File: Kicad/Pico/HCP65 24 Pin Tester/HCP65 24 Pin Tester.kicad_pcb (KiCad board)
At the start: 2 copper layers, 92 x 81.8 mm, 64 parts, among them IC1 SN74ABT245BDBR, IC2 SN74ABT245BDBR, IC3 SN74ABT245BDBR, J1 6339167-2, J3 Conn_01x12_Socket, J8 Conn_01x12_Socket, J9 Conn_01x12_Socket

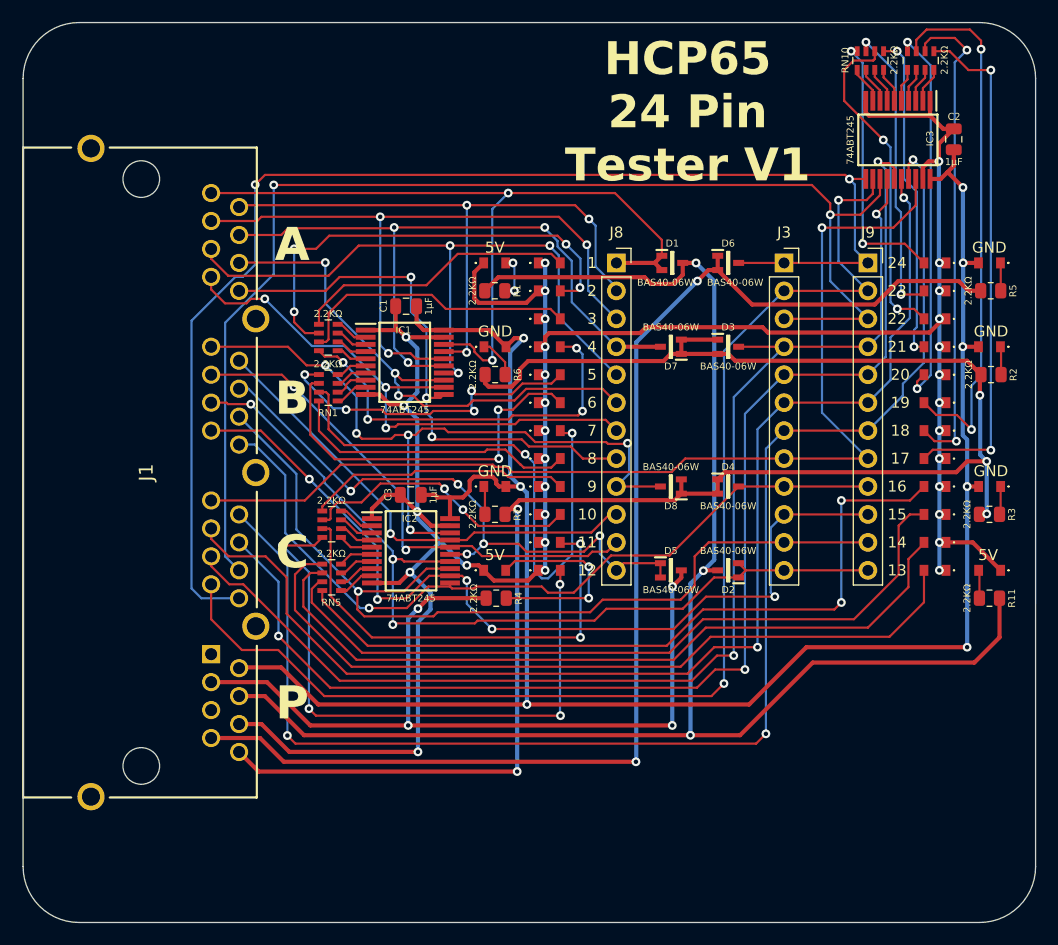
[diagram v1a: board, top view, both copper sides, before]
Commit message: Generated Gerbers for 24pin Tester.
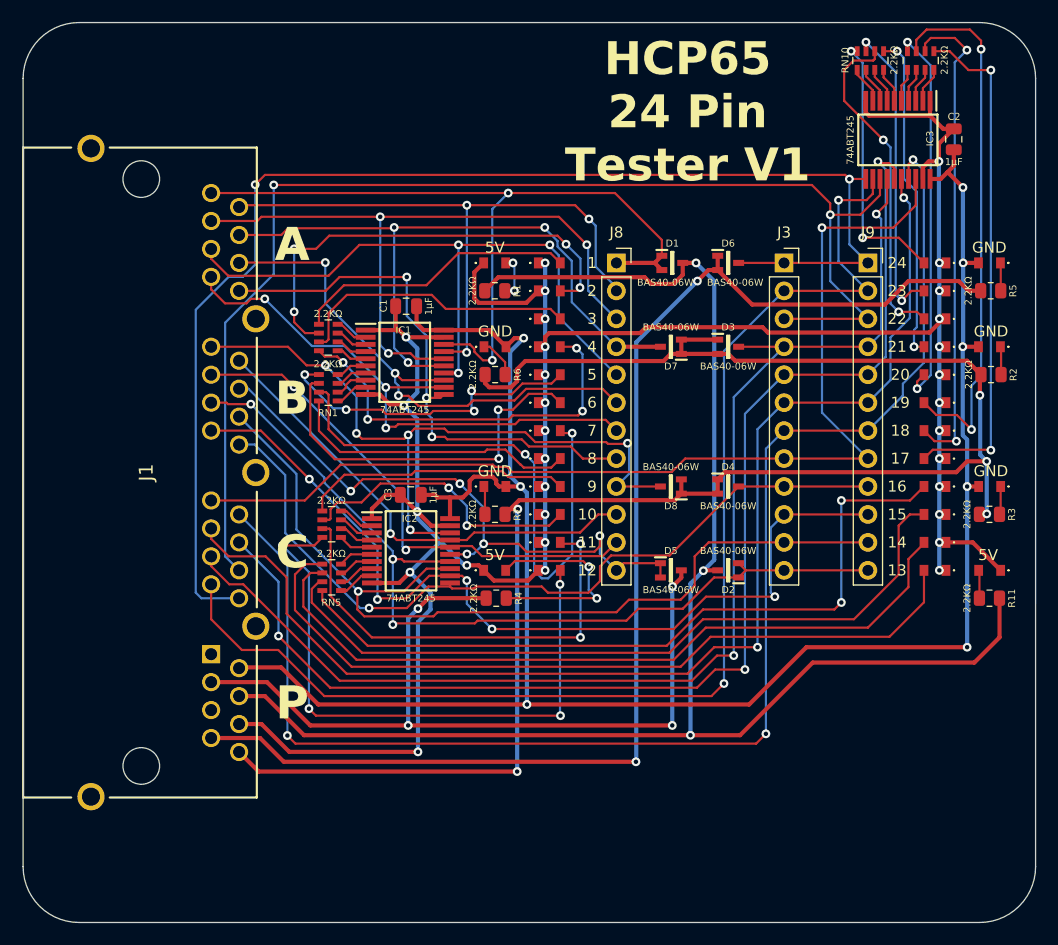
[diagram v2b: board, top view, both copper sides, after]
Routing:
- net Net-(LED5-Pad2): track 18.5 -> 19.5 mm
- net /S9: track 25.7 -> 26.5 mm
- net /IO15: track 71.9 -> 72.7 mm
- net /S22: track 27.3 -> 28.1 mm
- net /IO11: track 55.0 -> 55.7 mm
- net /IO9: track 42.5 -> 43.2 mm
- net /S8: track 24.0 -> 24.5 mm

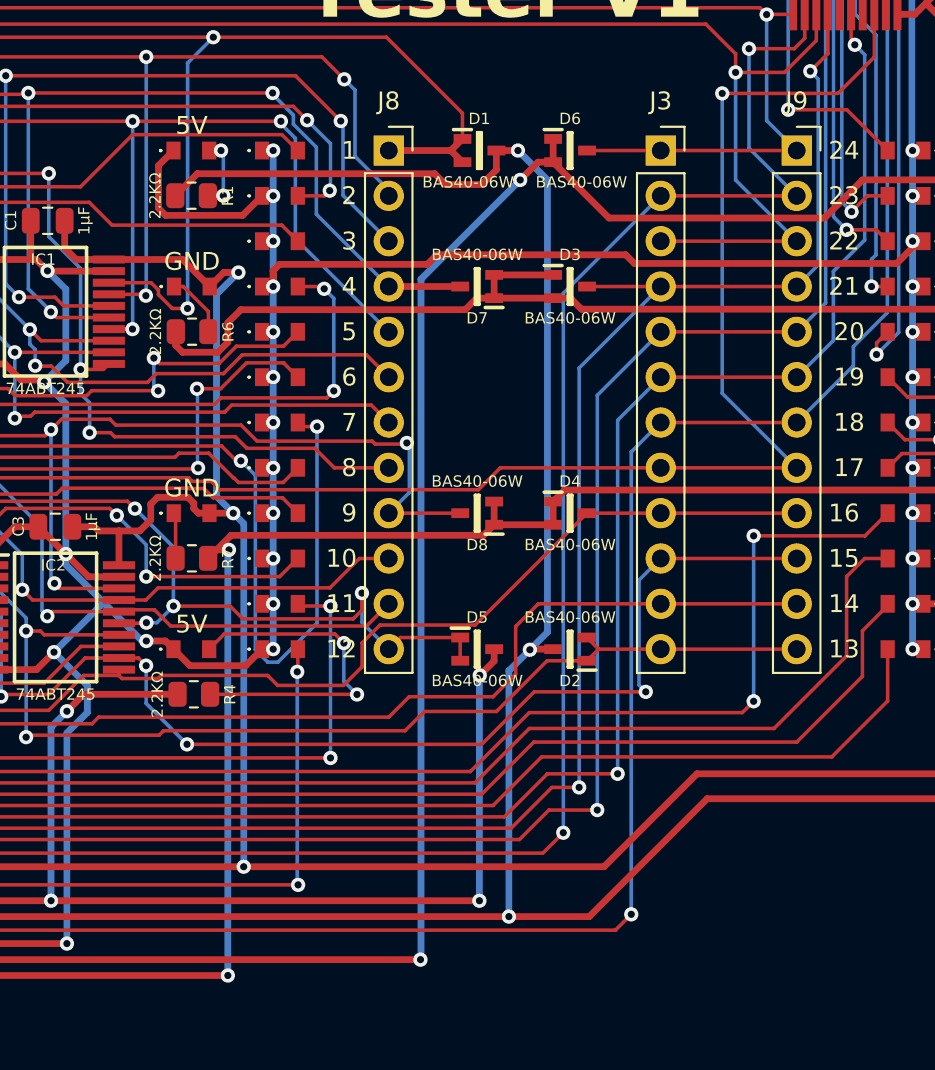
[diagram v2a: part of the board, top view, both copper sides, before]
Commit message: Added board alignment silk screen to 24- 32- and 40 pin tester boards.
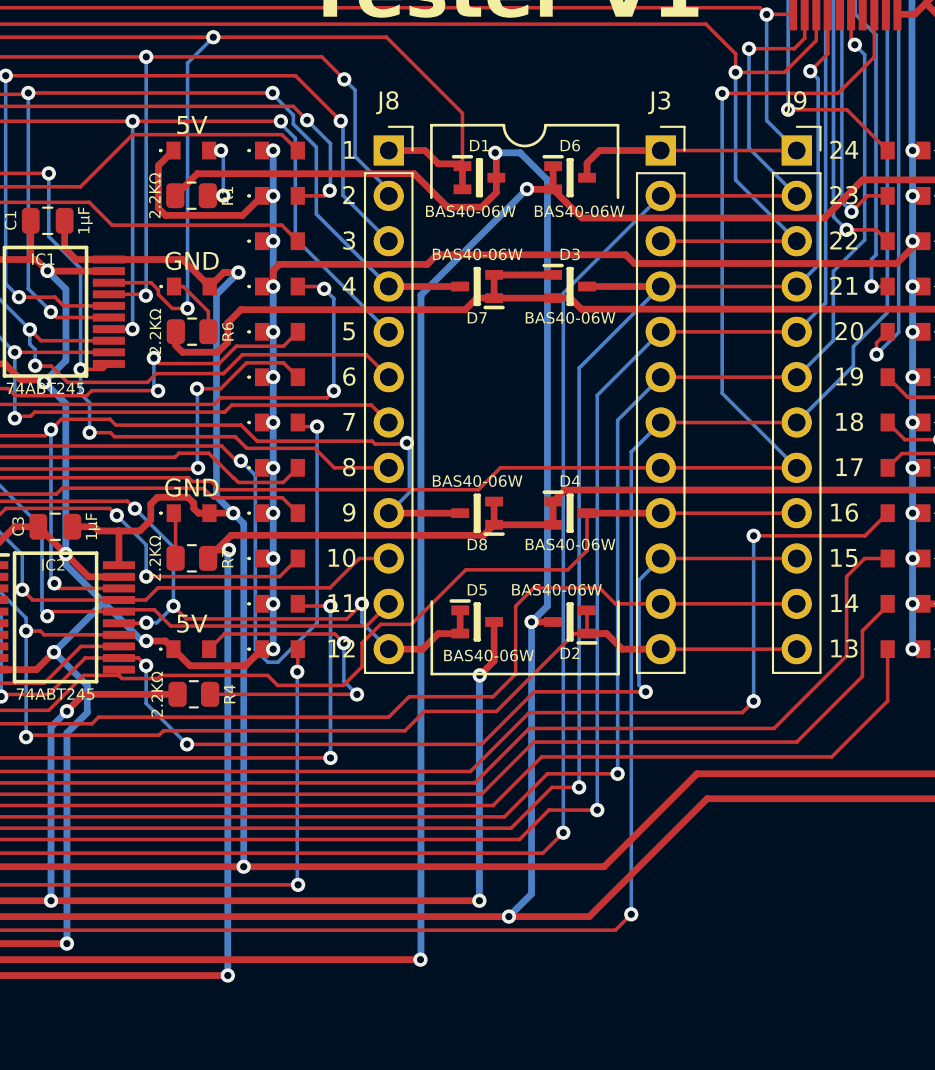
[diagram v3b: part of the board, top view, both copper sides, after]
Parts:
- moved D2 1.52 mm to (47.0, 32.8)
- moved D5 1.52 mm to (41.8, 32.8)
- moved D1 1.52 mm to (41.9, 7.87)
- moved D6 1.52 mm to (47.0, 7.87)
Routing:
- net /IO0: track 70.4 -> 72.4 mm
- net /GND_{2}: track 115.5 -> 113.7 mm
- net /5V_{1}: track 145.0 -> 146.6 mm
- net /5V_{2}: track 75.6 -> 77.1 mm
- net /IO13: track 82.2 -> 83.7 mm
- net /IO11: track 55.7 -> 54.4 mm
- net /IO15: track 72.7 -> 73.9 mm
- net /IO23: track 120.3 -> 121.4 mm
- net /IO12: track 80.5 -> 81.6 mm

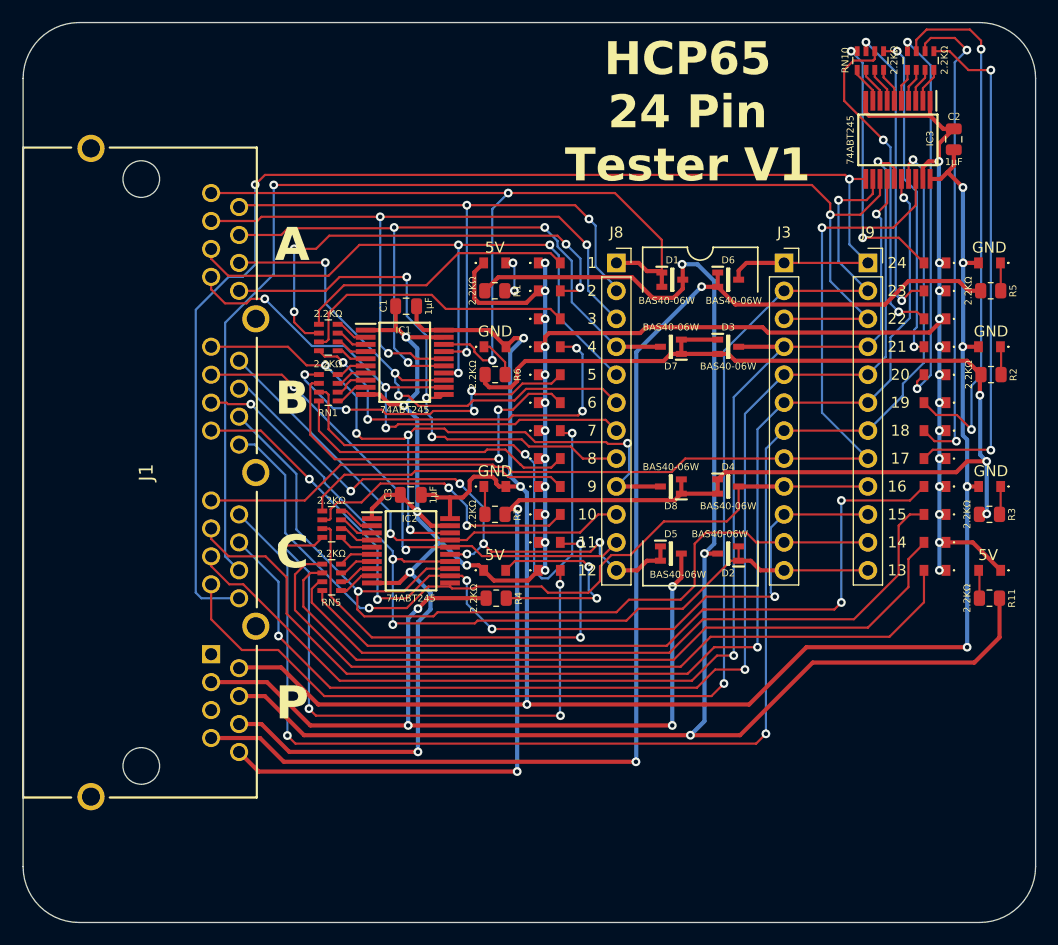
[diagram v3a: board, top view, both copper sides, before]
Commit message: Added debug points to Tester boards.
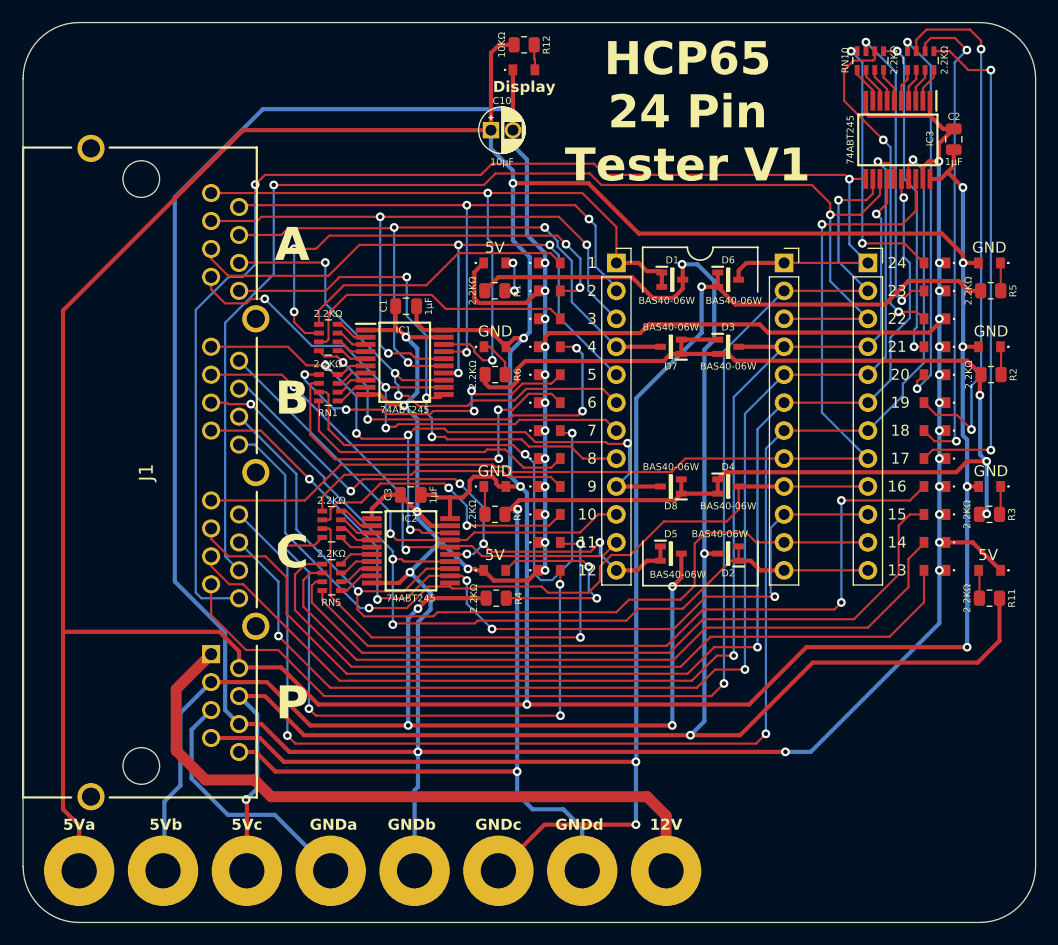
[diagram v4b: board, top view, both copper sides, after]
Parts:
- added C10: 10μF, SamacSys_Parts:CP_Radial_D4.0mm_P2.00mm, F.Cu at (25.4, -5.71)
- added H1: MountingHole_Pad, MountingHole:MountingHole_3.2mm_M3_Pad, F.Cu at (41.3, 61.6)
- added H2: MountingHole_Pad, MountingHole:MountingHole_3.2mm_M3_Pad, F.Cu at (-12.0, 61.6)
- added H3: MountingHole_Pad, MountingHole:MountingHole_3.2mm_M3_Pad, F.Cu at (-4.37, 61.6)
- added H4: MountingHole_Pad, MountingHole:MountingHole_3.2mm_M3_Pad, F.Cu at (3.25, 61.6)
- added H5: MountingHole_Pad, MountingHole:MountingHole_3.2mm_M3_Pad, F.Cu at (10.9, 61.6)
- added H6: MountingHole_Pad, MountingHole:MountingHole_3.2mm_M3_Pad, F.Cu at (26.1, 61.6)
- added H7: MountingHole_Pad, MountingHole:MountingHole_3.2mm_M3_Pad, F.Cu at (18.5, 61.6)
- added H8: MountingHole_Pad, MountingHole:MountingHole_3.2mm_M3_Pad, F.Cu at (33.7, 61.6)
- added LED49: 150224SS73100, SamacSys_Parts:150224SS73100A, F.Cu at (27.4, -11.2)
- added R12: 10KΩ, SamacSys_Parts:R_0805, F.Cu at (28.4, -13.5)
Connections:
- net /5V_{1} renamed /5Vc
- net /5V_{2} renamed /5Vb
- net /5V_{3} renamed /5Va
- net /GND_{1} renamed /GNDd
- net /GND_{2} renamed /GNDc
- net /GND_{3} renamed /GNDb
- J1 pad A5: /GND_{4} -> /GNDa
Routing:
- net /5Va: track 181.7 -> 371.5 mm, vias 8 -> 9
- net /GNDb: track 248.7 -> 421.5 mm, vias 31 -> 32
- net /12V: track 0.00 -> 62.1 mm
- net /GNDa: track 0.00 -> 23.1 mm
- net /GNDc: track 113.7 -> 133.7 mm, vias 2 -> 3
- net /5Vb: track 77.1 -> 95.9 mm
- net /5Vc: track 146.6 -> 163.8 mm, vias 3 -> 4
- net /GNDd: track 166.5 -> 179.6 mm
- net /IO0: track 72.4 -> 67.7 mm
- net Net-(LED49-Pad2): track 0.00 -> 2.30 mm
- net /IO21: track 114.9 -> 115.8 mm
- net /IO23: track 121.4 -> 122.3 mm
- net /S6: track 50.4 -> 51.0 mm
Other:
- board text added: "12V"
- board text added: "5Va"
- board text added: "5Vb"
- board text added: "5Vc"
- board text added: "Display"
- board text added: "GNDa"
- board text added: "GNDb"
- board text added: "GNDc"
- board text added: "GNDd"

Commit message: Started fixing 24, 32 and 40 pin Tester Boards.
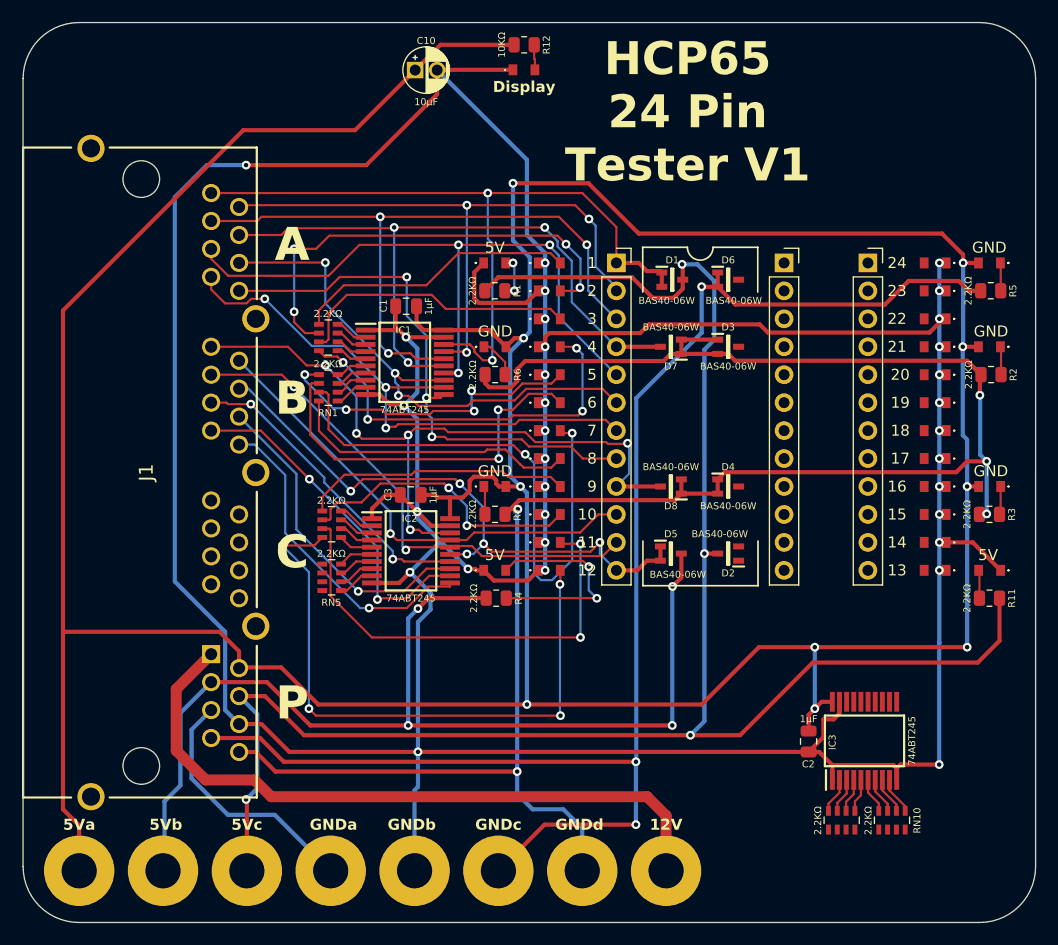
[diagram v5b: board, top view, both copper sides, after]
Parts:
- moved RN9 69.5 mm to (57.3, 57.0), turned to 90 degrees
- moved RN10 69.1 mm to (61.9, 57.0), turned to 90 degrees
- moved C2 56.3 mm to (54.3, 49.8), turned to 180 degrees
- moved IC3 54.7 mm to (59.4, 49.8), turned to 90 degrees
- moved LED19 27.9 mm to (66.8, 6.35)
- moved LED24 27.9 mm to (66.8, 34.3)
- moved LED18 22.9 mm to (66.8, 8.89)
- moved LED25 22.9 mm to (66.8, 31.8)
- moved LED17 17.8 mm to (66.8, 11.4)
- moved LED26 17.8 mm to (66.8, 29.2)
- moved LED16 12.7 mm to (66.8, 14.0)
- moved LED27 12.7 mm to (66.8, 26.7)
- moved C10 8.79 mm to (18.5, -11.2)
- moved LED28 7.62 mm to (66.8, 24.1)
- moved LED31 7.62 mm to (66.8, 16.5)
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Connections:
- D2 pad 1: /IO12 -> /IO23
- D2 pad 2: /IO12 -> /IO23
- D3 pad 3: /IO20 -> /IO15
- D4 pad 3: /IO15 -> /IO20
- D6 pad 3: /IO23 -> /IO12
- IC3 pad 11: /IO23 -> /IO16
- IC3 pad 12: /IO22 -> /IO17
- IC3 pad 13: /IO21 -> /IO18
- IC3 pad 14: /IO20 -> /IO19
- IC3 pad 15: /IO19 -> /IO20
- IC3 pad 16: /IO18 -> /IO21
- IC3 pad 17: /IO17 -> /IO22
- IC3 pad 18: /IO16 -> /IO23
- J3 pad 1: /IO23 -> /IO12
- J3 pad 10: /IO14 -> /IO21
- J3 pad 11: /IO13 -> /IO22
- J3 pad 12: /IO12 -> /IO23
- J3 pad 2: /IO22 -> /IO13
- J3 pad 3: /IO21 -> /IO14
- J3 pad 4: /IO20 -> /IO15
- J3 pad 5: /IO19 -> /IO16
- J3 pad 6: /IO18 -> /IO17
- J3 pad 7: /IO17 -> /IO18
- J3 pad 8: /IO16 -> /IO19
- J3 pad 9: /IO15 -> /IO20
- J9 pad 1: /IO23 -> /IO12
- J9 pad 10: /IO14 -> /IO21
- J9 pad 11: /IO13 -> /IO22
- J9 pad 12: /IO12 -> /IO23
- J9 pad 2: /IO22 -> /IO13
- J9 pad 3: /IO21 -> /IO14
- J9 pad 4: /IO20 -> /IO15
- J9 pad 5: /IO19 -> /IO16
- J9 pad 6: /IO18 -> /IO17
- J9 pad 7: /IO17 -> /IO18
- J9 pad 8: /IO16 -> /IO19
- J9 pad 9: /IO15 -> /IO20
- RN10 pad 5: /S20 -> /S19
- RN10 pad 6: /S21 -> /S18
- RN10 pad 7: /S22 -> /S17
- RN10 pad 8: /S23 -> /S16
- RN9 pad 5: /S16 -> /S23
- RN9 pad 6: /S17 -> /S22
- RN9 pad 7: /S18 -> /S21
- RN9 pad 8: /S19 -> /S20
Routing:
- net /IO17: track 131.0 -> 0.00 mm, vias 3 -> 0
- net /IO23: track 122.3 -> 0.00 mm, vias 2 -> 0
- net /IO21: track 115.8 -> 0.00 mm, vias 2 -> 0
- net /IO19: track 113.9 -> 0.00 mm, vias 3 -> 0
- net /IO22: track 112.6 -> 0.00 mm, vias 2 -> 0
- net /IO20: track 111.7 -> 0.00 mm, vias 2 -> 0
- net /IO18: track 111.7 -> 0.00 mm, vias 2 -> 0
- net /IO16: track 96.8 -> 0.00 mm, vias 1 -> 0
- net /S12: track 70.7 -> 0.00 mm
- net /S15: track 68.7 -> 0.00 mm, vias 2 -> 0
- net /S13: track 68.7 -> 0.00 mm
- net /S14: track 68.0 -> 0.00 mm
- net /IO13: track 83.7 -> 29.6 mm
- net /IO12: track 81.6 -> 28.4 mm, vias 3 -> 2
- net /IO14: track 81.5 -> 31.8 mm, vias 5 -> 2
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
